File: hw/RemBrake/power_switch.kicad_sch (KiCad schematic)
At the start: 44 parts, among them Q1 SiS415DNT, Q2 BC337, Q3 BC847, Q4 BC337, Q5 BC847, U1 TPS62140, U2 BD48ExxG, U3 XC6220B331MR, U4 MAX40200AUK

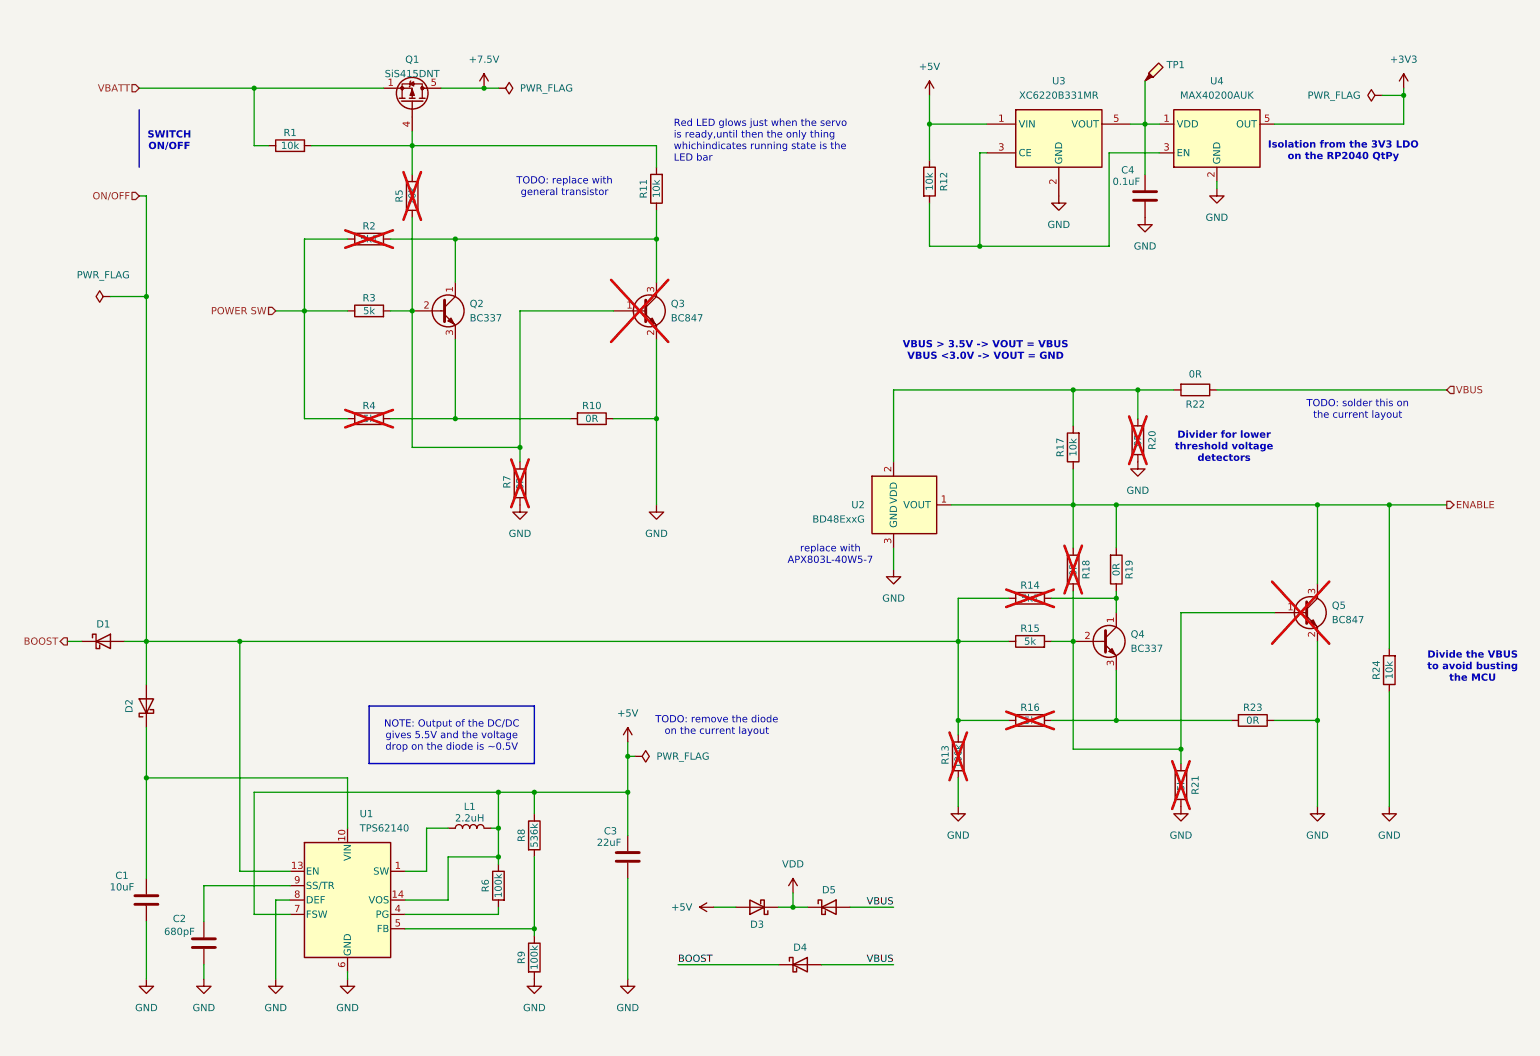
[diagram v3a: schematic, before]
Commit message: schematics update
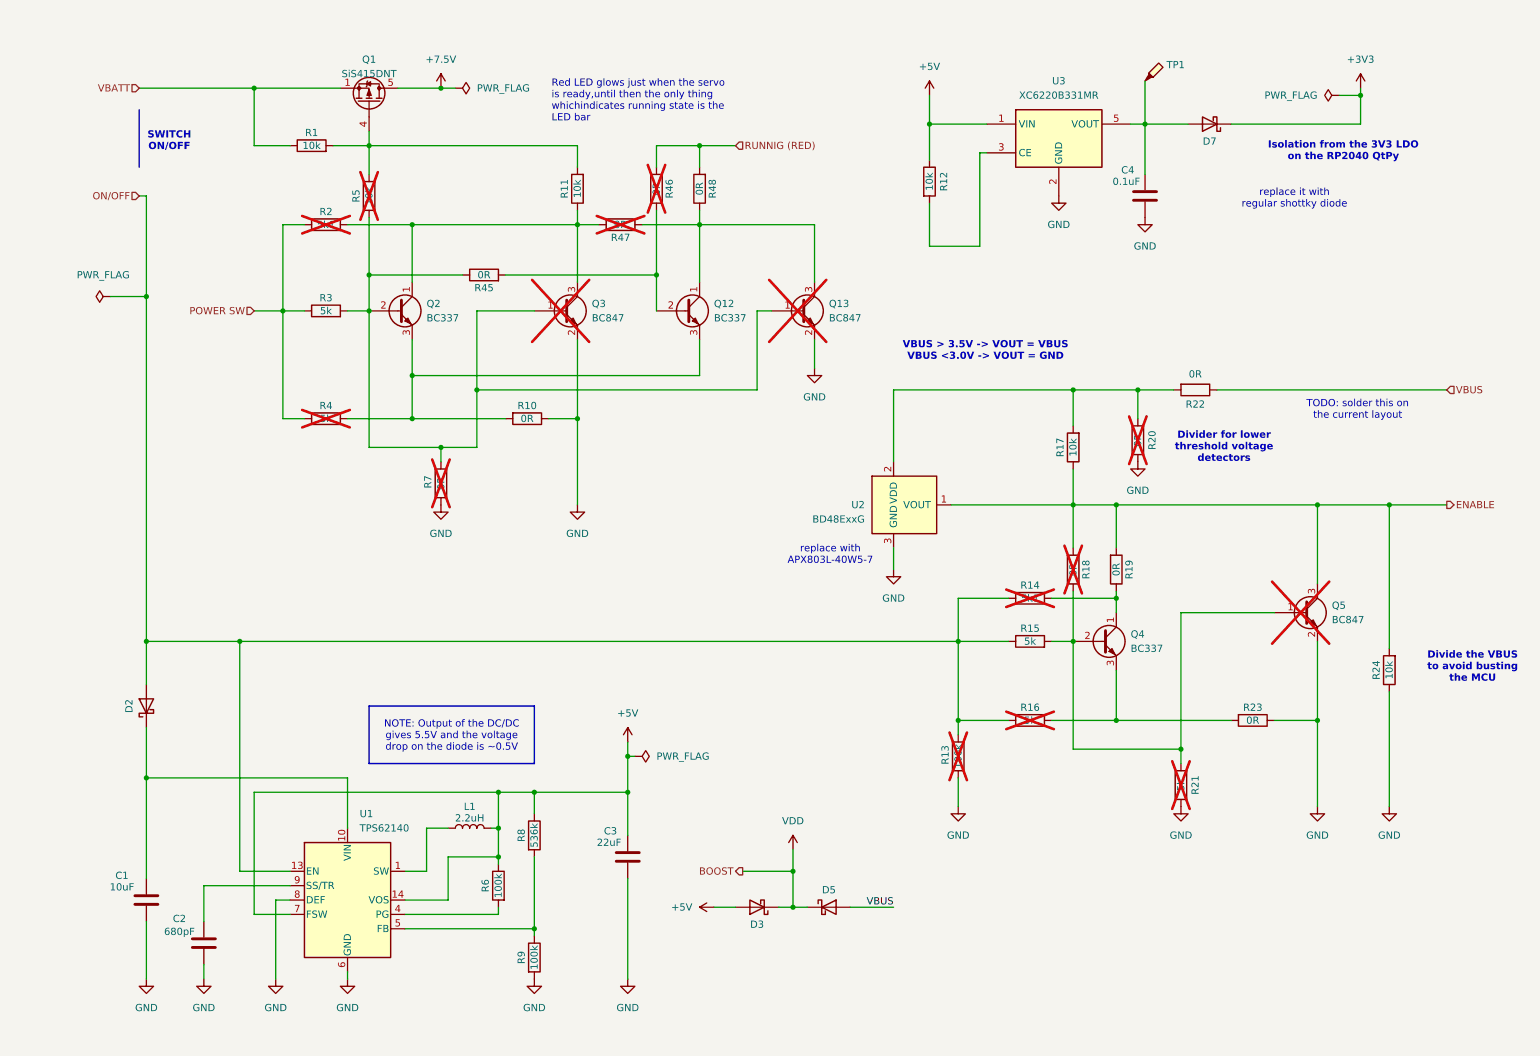
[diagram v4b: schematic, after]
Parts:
- removed D1, D4: MBR0520, Diode_SMD:D_SOD-123, symbol Device:D_Schottky
- removed U4: MAX40200AUK, Package_TO_SOT_SMD:SOT-23-5, symbol Analog_Switch:MAX40200AUK
- added D7: MBR0520, Diode_SMD:D_SOD-123, symbol Device:D_Schottky
- added Q12: BC337, Package_TO_SOT_THT:TO-92_Inline, symbol Transistor_BJT:BC337
- added Q13: BC847, Package_TO_SOT_SMD:SOT-23, symbol Transistor_BJT:BC847
- added R45, R46, R47, R48: 0R, Resistor_SMD:R_0805_2012Metric_Pad1.20x1.40mm_HandSolder, symbol Device:R
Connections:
- net +3V3: now also D7.1 (K)
- net GND: now also Q13.2 (E)
- net at Q2.1 (C), Q3.3 (C), R11.1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: now also R47.1
- net at Q2.2 (B), Q3.1 (B), R3.2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: now also Q13.1 (B), R45.1
- net at Q2.3 (E), R10.2, R4.2: now also Q12.3 (E)
- net at C4.1, TP1.1, U3.5 (VOUT): now also D7.2 (A)
- new net: Q12.1 (C), Q13.3 (C), R47.2, R48.1
- new net: Q12.2 (B), R45.2, R46.1
- new net RUNNIG (RED): R46.2, R48.2
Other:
- note added: "replace it with regular shottky diode"
- note removed: "TODO: remove the diode on the current layout"
- note removed: "TODO: replace with general transistor"
- moved on the sheet: Q1, Q2, Q3, R1, R10, R11, R2, R3, R4, R5, R7

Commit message: finished todos - prepared for routing
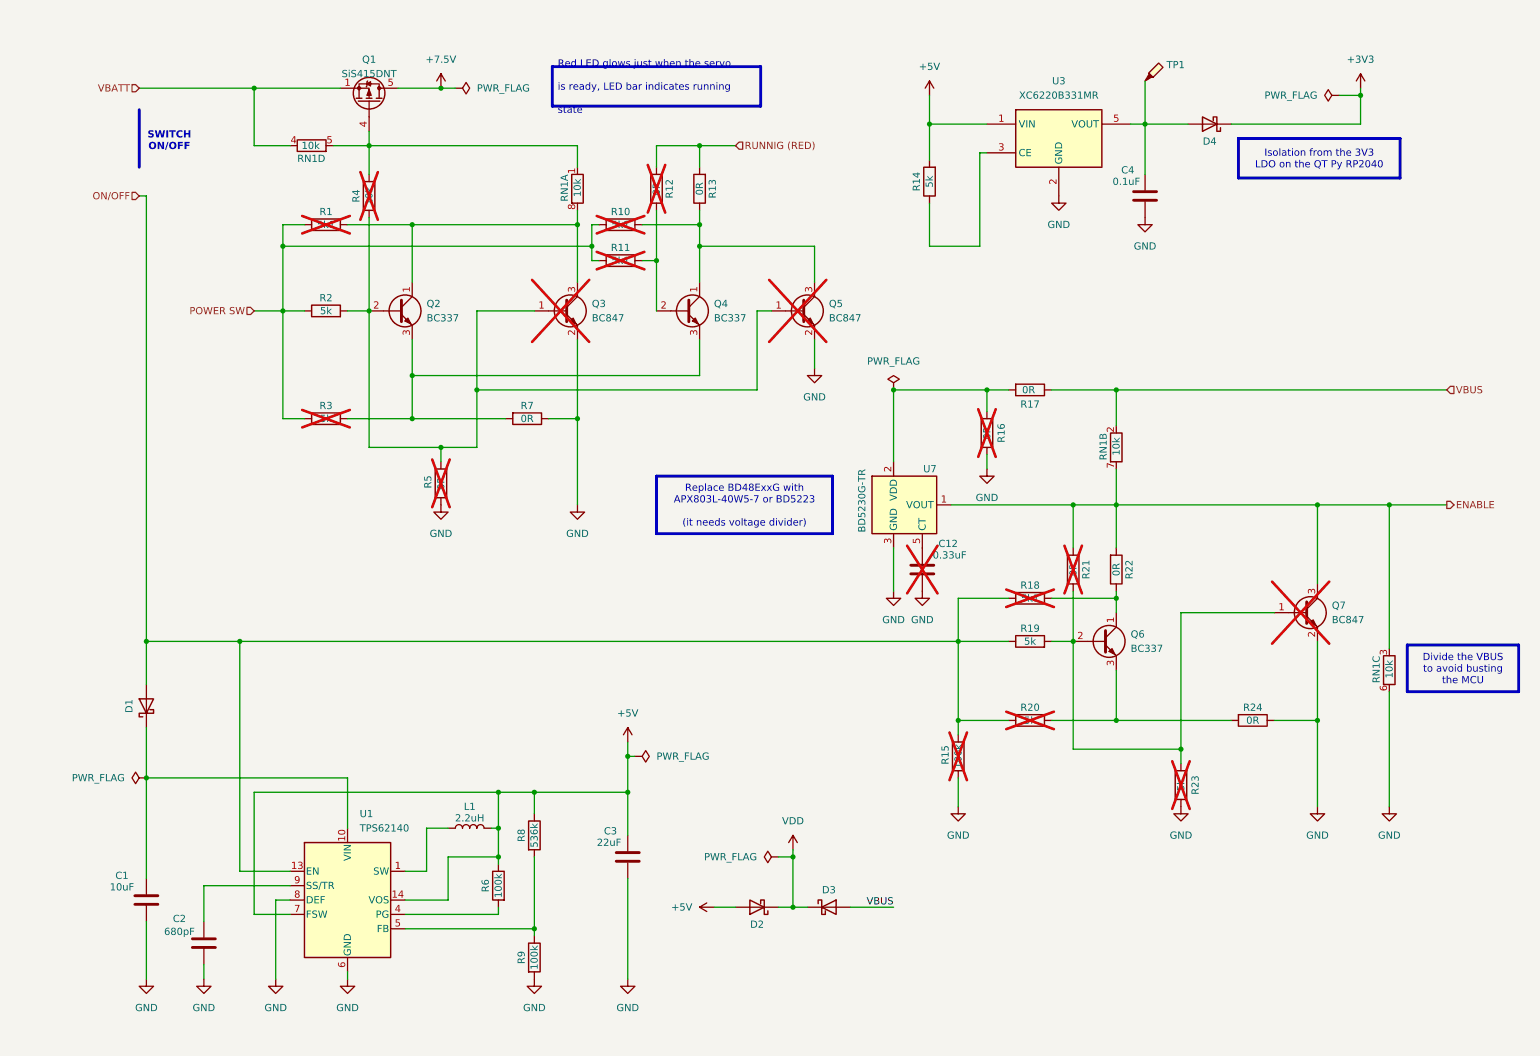
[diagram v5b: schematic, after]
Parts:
- removed R12, R17, R24: 10k, Resistor_SMD:R_0805_2012Metric_Pad1.20x1.40mm_HandSolder, symbol Device:R
- removed R45, R47: 0R, Resistor_SMD:R_0805_2012Metric_Pad1.20x1.40mm_HandSolder, symbol Device:R
- removed U2: BD48ExxG, Package_TO_SOT_SMD:SOT-23-5, symbol Power_Management:BD48ExxG
- added C12: 0.33uF, Capacitor_SMD:C_0805_2012Metric_Pad1.18x1.45mm_HandSolder, symbol Device:C
- added R10: 5k1, Resistor_SMD:R_0805_2012Metric_Pad1.20x1.40mm_HandSolder, symbol Device:R
- added RN1: 10k, Resistor_SMD:R_Array_Convex_4x0603, symbol Device:R_Pack04_Split
- added U7: BD5230G-TR, Package_TO_SOT_SMD:SOT-23-5, symbol dodo-power:BD5230G-TR
- D1: renamed from D2; Purchase https://cz.farnell.com/diodes-inc/mbr230s1f-7/schottky-rect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 -> (none)
- D2: renamed from D3; Purchase https://cz.farnell.com/diodes-inc/mbr230s1f-7/schottky-rect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 -> (none)
- D3: renamed from D5; Purchase https://cz.farnell.com/diodes-inc/mbr230s1f-7/schottky-rect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 -> (none)
- D4: renamed from D7; Purchase https://cz.farnell.com/diodes-inc/mbr230s1f-7/schottky-rect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 -> (none)
- L1: Purchase https://cz.farnell.com/murata/dfe252012p-2r2m-p2/inductor-2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 -> (none)
- R11: value 10k -> 5k1; now not fitted; now left out of the parts list
- R14: renamed from R1; value 10k -> 5k
- renumbered Q12 to Q4, Q13 to Q5, Q4 to Q6, Q5 to Q7, R2 to R1, R46 to R12, R48 to R13, R13 to R15, R20 to R16, R22 to R17, R14 to R18, R15 to R19, R3 to R2, R16 to R20, R18 to R21, R19 to R22, R21 to R23, R23 to R24, R4 to R3, R5 to R4, R7 to R5, R10 to R7
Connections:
- net +5V: now also R14.2
- net ENABLE: now also RN1.3 (R3.1), RN1.7 (R2.2), U7.1 (VOUT)
- net GND: now also C12.2, RN1.6 (R3.2), U7.3 (GND)
- net POWER SW: now also R11.1, R10.1
- net VBATT: now also RN1.4 (R4.1); no longer R14.1
- net VBUS: now also RN1.2 (R2.1)
- net at Q2.1 (C), Q3.3 (C), R1.2: now also RN1.8 (R1.2); no longer R11.1
- net at Q4.1 (C), Q5.3 (C), R13.1: now also R10.2
- net at Q4.2 (B), R12.1: now also R11.2
- net at U3.3 (CE): now also R14.1
- net at Q1.4 (G), R4.2: now also RN1.1 (R1.1), RN1.5 (R4.2); no longer R11.2, R14.2
- net at R16.1, R17.2: now also U7.2 (VDD)
- new net: C12.1, U7.5 (CT)
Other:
- note removed: "Divide the VBUS to avoid busting the MCU"
- note removed: "Divider for lower threshold voltage detectors"
- note removed: "Isolation from the 3V3 LDO on the RP2040 QtPy"
- note removed: "Red LED glows just when the servo is ready,until then the only thing whichindicates running state is the LED bar"
- note removed: "TODO: solder this on the current layout"
- note removed: "VBUS > 3.5V -> VOUT = VBUS VBUS <3.0V -> VOUT = GND"
- note removed: "replace it with regular shottky diode"
- note removed: "replace with APX803L-40W5-7"
- moved on the sheet: R14, R16, R17

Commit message: new routing version 3.0 with power mosfet swich for the charger and fixed problems with LED and buzzer reset delayed circuit
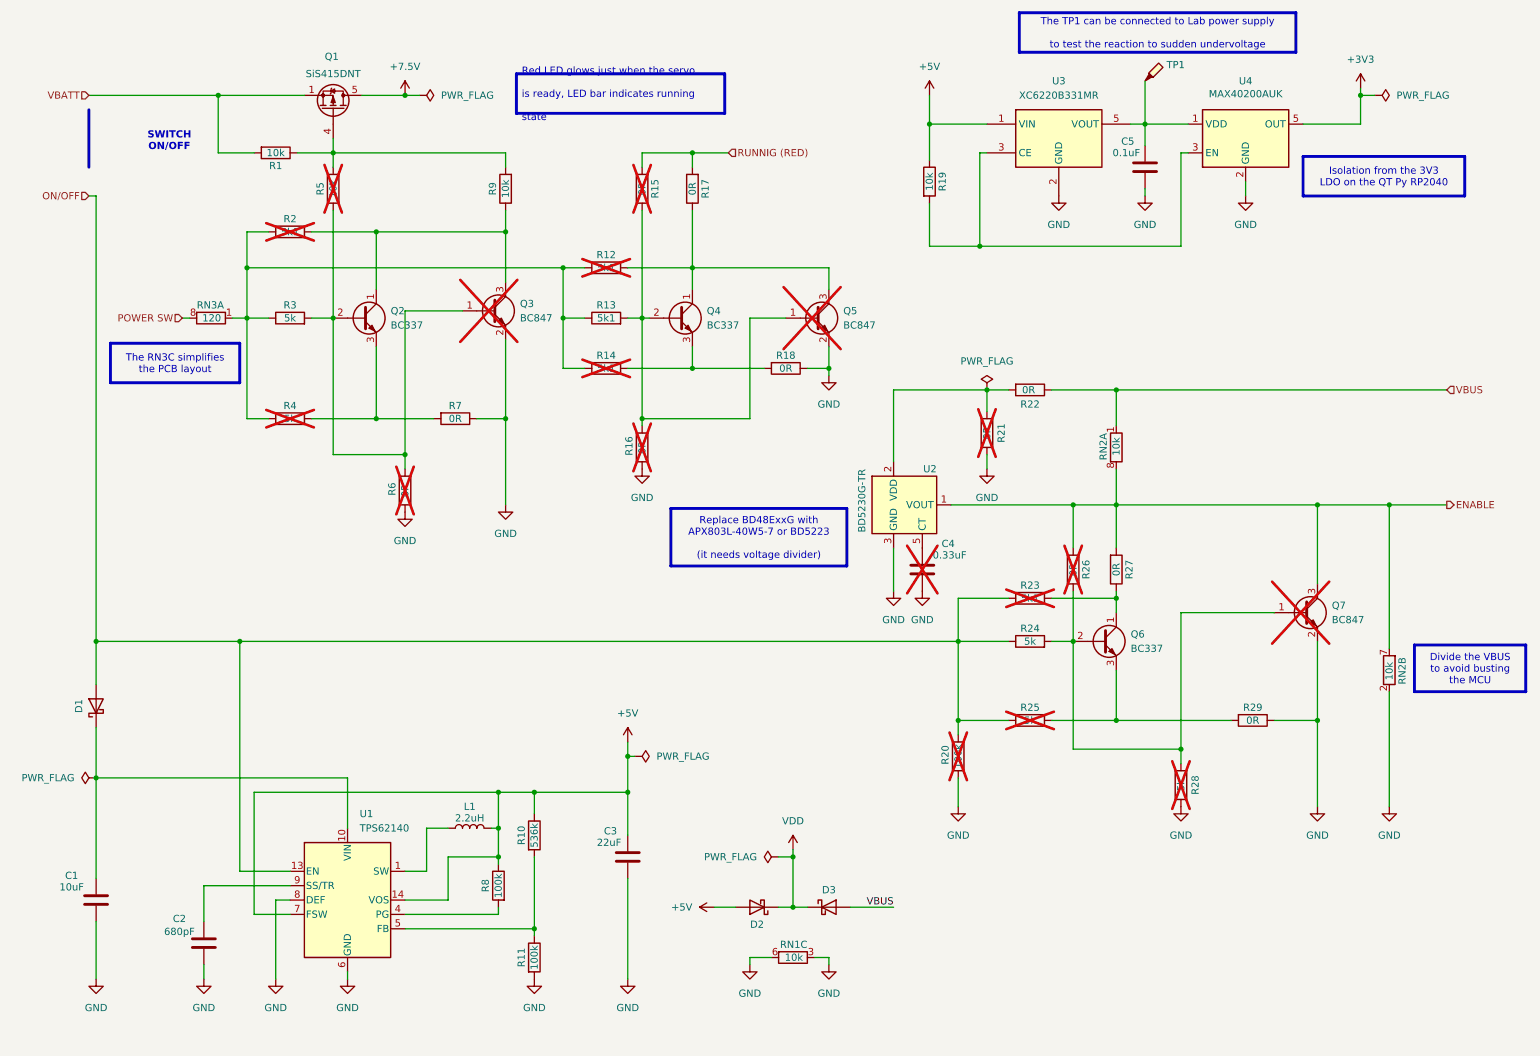
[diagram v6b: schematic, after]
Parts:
- removed D4: MBR0520, Diode_SMD:D_SOD-123, symbol Device:D_Schottky
- removed unit 1 of RN1
- removed unit 4 of RN1
- removed unit 2 of RN1
- added R1, R19: 10k, Resistor_SMD:R_0805_2012Metric_Pad1.20x1.40mm_HandSolder, symbol Device:R
- added R14: 5k1, Resistor_SMD:R_0805_2012Metric_Pad1.20x1.40mm_HandSolder, symbol Device:R
- added R16, R18: 0R, Resistor_SMD:R_0805_2012Metric_Pad1.20x1.40mm_HandSolder, symbol Device:R
- added RN2: 10k, Resistor_SMD:R_Array_Convex_4x0603, symbol Device:R_Pack04_Split
- added RN3: 120, Resistor_SMD:R_Array_Concave_4x0603, symbol Device:R_Pack04_Split
- added U4: MAX40200AUK, Package_TO_SOT_SMD:SOT-23-5, symbol Analog_Switch:MAX40200AUK
- R13: renamed from R11; now fitted; now in the parts list
- R9: renamed from R14; value 5k -> 10k
- renumbered C12 to C4, C4 to C5, R8 to R10, R9 to R11, R10 to R12, R12 to R15, R13 to R17, R1 to R2, R15 to R20, R16 to R21, R17 to R22, R18 to R23, R19 to R24, R20 to R25, R21 to R26, R22 to R27, R23 to R28, R24 to R29, R2 to R3, R3 to R4, R4 to R5, R5 to R6, R6 to R8, U7 to U2
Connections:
- net +3V3: now also U4.5 (OUT)
- net +5V: now also R19.1; no longer R9.2
- net ENABLE: now also RN2.7 (R2.2), RN2.8 (R1.2); no longer RN1.3 (R3.1)
- net GND: now also RN1.3 (R3.1), R16.1, R18.1, RN2.2 (R2.1), U4.2 (GND)
- net POWER SW: now also RN3.8 (R1.2); no longer R12.1, R13.1, R2.1, R3.1, R4.1
- net VBATT: now also R1.2
- net VBUS: now also RN2.1 (R1.1)
- net at Q2.1 (C), Q3.3 (C), R2.2: now also R9.1
- net at Q2.2 (B), Q3.1 (B), R3.2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: no longer Q5.1 (B)
- net at Q2.3 (E), R4.2, R7.2: no longer Q4.3 (E)
- net at Q4.2 (B), R13.2, R15.1: now also Q5.1 (B), R16.2
- net at U3.3 (CE): now also R19.2, U4.3 (EN); no longer R9.1
- net at Q1.4 (G), R5.2: now also R9.2, R1.1
- net at C5.1, TP1.1, U3.5 (VOUT): now also U4.1 (VDD)
- new net: Q4.3 (E), R14.2, R18.2
- new net: R12.1, R13.1, R14.1, R2.1, R3.1, R4.1, RN3.1 (R1.1)
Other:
- moved on the sheet: C1, C5, D1, Q1, Q2, Q3, Q4, Q5, R12, R15, R17, R2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
